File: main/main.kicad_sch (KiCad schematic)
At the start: 43 parts, among them J1 JST PH, J2 JST SH, J3 USB_C_Receptacle_USB2.0, J4 TC2030_SWD, Q1 DMG3413L, Q2 DMG3413L, U1 TPS61092, U2 WE-TVS-82400102, U3 MCP73831-2-OT, U4 SN74LV1T34DBV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

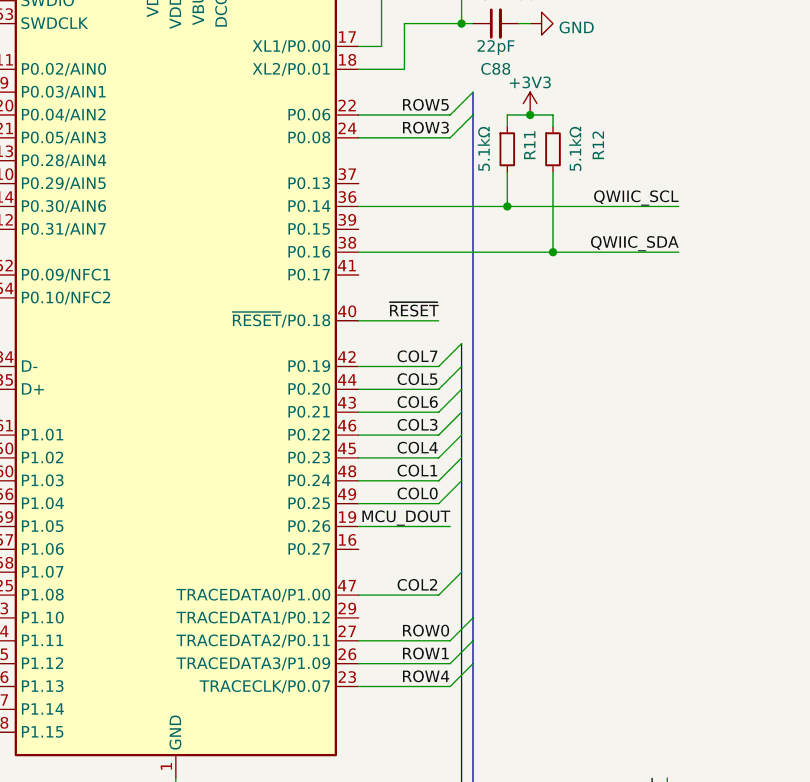
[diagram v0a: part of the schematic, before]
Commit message: Connect power managment to MCU
i don't like it but hopefully it will work
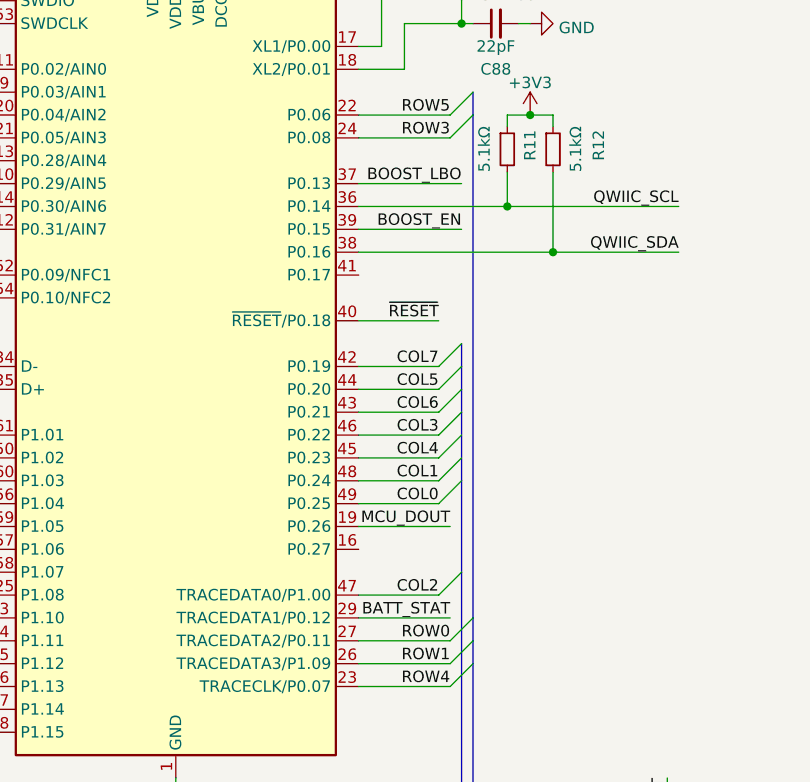
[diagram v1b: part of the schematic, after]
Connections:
- net BATT_STAT: now also U5.29 (TRACEDATA1/P0.12)
- net BOOST_EN: now also U5.39 (P0.15)
- net BOOST_LBO: now also U5.37 (P0.13)
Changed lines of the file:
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@@
+    (stroke (width 0) (type default) (color 0 0 0 0))
+  )
+  (wire (pts (xy 168.91 73.66) (xy 180.34 73.66))
     (stroke (width 0) (type default) (color 0 0 0 0))
   )
@@
     (stroke (width 0) (type default) (color 0 0 0 0))
   )
+  (wire (pts (xy 168.91 78.74) (xy 180.34 78.74))
+    (stroke (width 0) (type default) (color 0 0 0 0))
+  )
   (wire (pts (xy 241.3 77.47) (xy 240.03 77.47))
     (stroke (width 0) (type default) (color 0 0 0 0))
@@
     (stroke (width 0) (type default) (color 0 0 0 0))
   )
+  (wire (pts (xy 168.91 121.92) (xy 179.07 121.92))
+    (stroke (width 0) (type default) (color 0 0 0 0))
+  )
   (wire (pts (xy 193.04 151.13) (xy 193.04 149.86))
     (stroke (width 0) (type default) (color 0 0 0 0))
@@
     (effects (font (size 1.27 1.27)) (justify right bottom))
   )
+  (label "BOOST_LBO" (at 180.34 73.66 180)
+    (effects (font (size 1.27 1.27)) (justify right bottom))
+  )
   (label "VUSB" (at 187.96 149.86 0)
     (effects (font (size 1.27 1.27)) (justify left bottom))
@@
     (effects (font (size 1.27 1.27)) (justify right bottom))
   )
+  (label "BOOST_EN" (at 180.34 78.74 180)
+    (effects (font (size 1.27 1.27)) (justify right bottom))
+  )
+  (label "BATT_STAT" (at 179.07 121.92 180)
+    (effects (font (size 1.27 1.27)) (justify right bottom))
+  )
